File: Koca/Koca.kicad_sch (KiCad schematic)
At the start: 160 parts, among them J1 USB_C_Receptacle, J2 AudioJack4, J3 Conn_01x04_Pin, J4 Conn_01x04_Pin, J5 USB_C_Receptacle, J6 AudioJack4, J7 Conn_01x04_Pin, J8 Conn_01x04_Pin, SW1 SW_Push, SW10 SW_Push, SW11 SW_Push, SW12 SW_Push, SW13 SW_Push, SW14 SW_Push, SW15 SW_Push, SW16 SW_Push, SW17 SW_Push, SW18 SW_Push, SW19 SW_Push, SW2 SW_Push, SW20 SW_Push, SW21 SW_Push, SW22 SW_Push, SW23 SW_Push, SW24 SW_Push, SW25 SW_Push, SW26 SW_Push, SW27 SW_Push, SW28 SW_Push, SW29 SW_Push, SW3 SW_Push, SW30 SW_Push, SW31 SW_Push, SW32 SW_Push, SW33 SW_Push, SW34 SW_Push, SW35 SW_Push, SW36 SW_Push, SW37 SW_Push, SW38 SW_Push, SW39 SW_Push, SW4 SW_Push, SW40 SW_Push, SW41 SW_Push, SW42 SW_Push, SW43 SW_Push, SW44 SW_Push, SW45 SW_Push, SW46 SW_Push, SW47 SW_Push, SW48 SW_Push, SW49 SW_Push, SW5 SW_Push, SW50 SW_Push, SW51 SW_Push, SW52 SW_Push, SW53 SW_Push, SW54 SW_Push, SW55 SW_Push, SW56 SW_Push, SW57 SW_Push, SW58 SW_Push, SW59 SW_Push, SW6 SW_Push, SW60 SW_Push, SW7 SW_Push, SW8 SW_Push, SW9 SW_Push, U1 AMS1117-3.3, U2 USBLC6-2SC6, U3 USBLC6-2SC6, U4 STM32F103RCTx, U5 AMS1117-3.3, U6 USBLC6-2SC6, U7 USBLC6-2SC6, U8 STM32F103RCTx, Y1 12Mhz, Y2 12Mhz

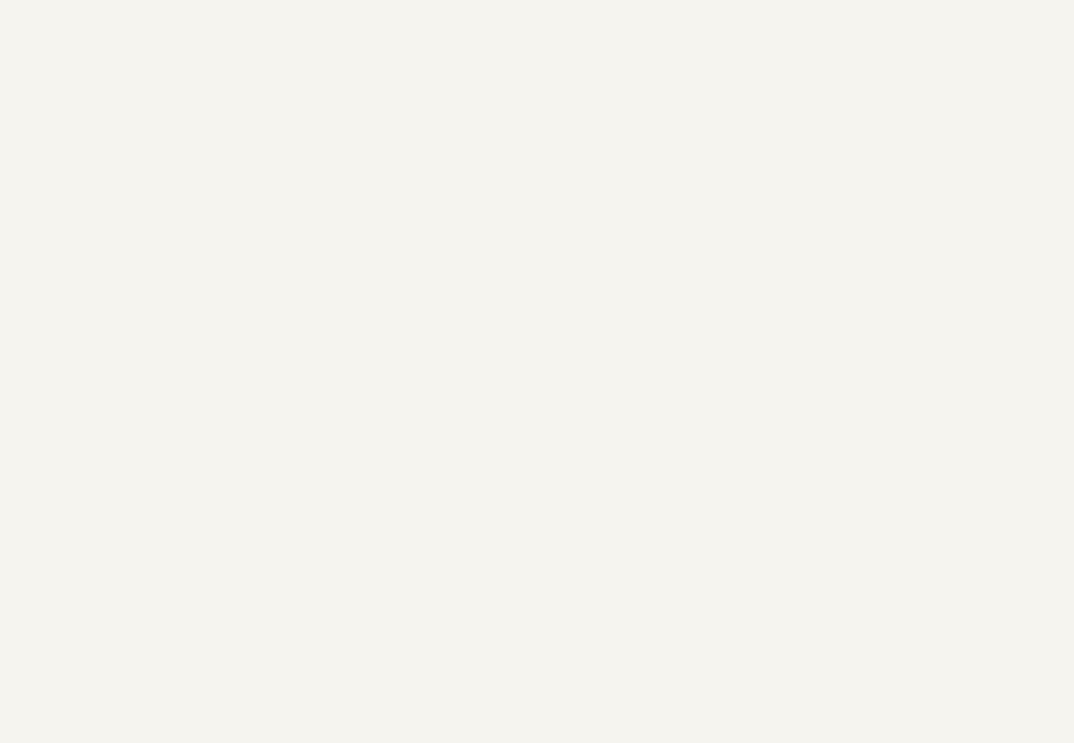
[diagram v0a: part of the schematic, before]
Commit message: Bout to imrpove hotplug protection
Making a commit now because I have some new changes and I want something
to fall back on if the new design changes suck.
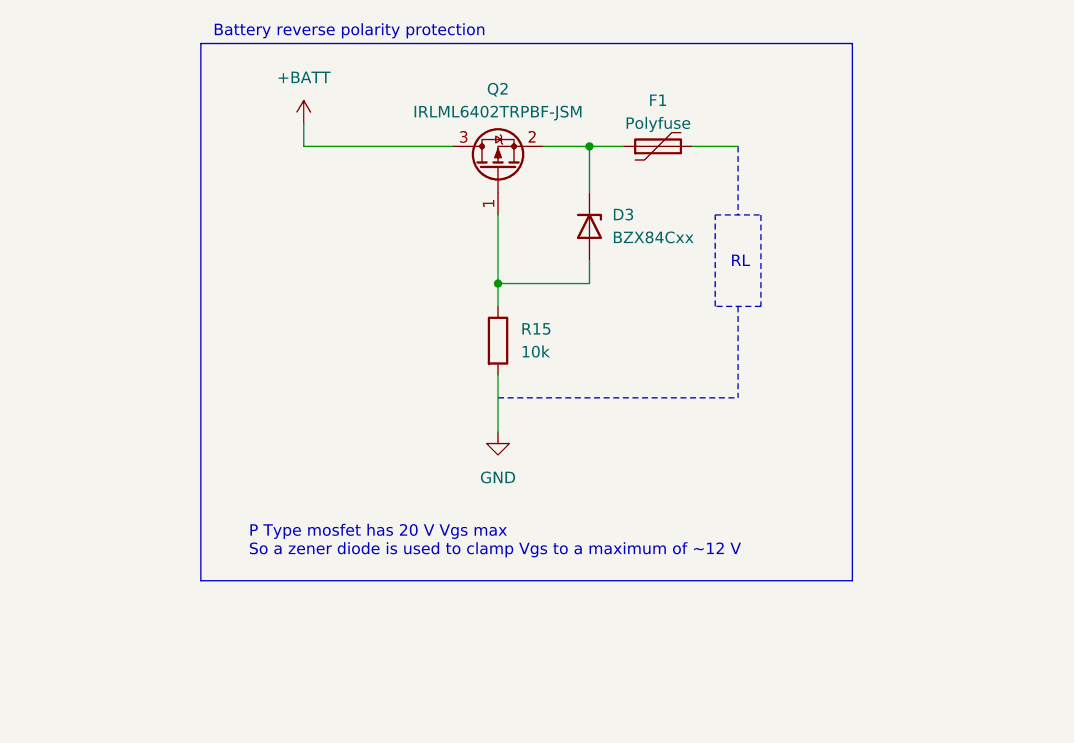
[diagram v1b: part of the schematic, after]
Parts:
- added D3: BZX84Cxx, Package_TO_SOT_SMD:SOT-23, symbol Diode:BZX84Cxx
- added F1: Polyfuse, symbol Device:Polyfuse
- added Q2: IRLML6402TRPBF-JSM, Package_TO_SOT_SMD:SOT-23, symbol Transistor_FET:AO3401A
- added R15: 10k, Resistor_SMD:R_0603_1608Metric, symbol Device:R
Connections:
- net GND: now also R15.2
- new net: D3.1 (A), Q2.1 (G), R15.1
- new net: D3.3 (K), F1.1, Q2.2 (S)
- new net +BATT: Q2.3 (D)
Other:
- note added: "Battery reverse polarity protection"
- note added: "P Type mosfet has 20 V Vgs max So a zener diode is used to clamp Vgs to a maximum of ~12 V"
- note added: "RL"

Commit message: Added hotplugging protection to TRRS
Technically added hotplugging protection. But it won't work because
current isn't able to flow both directions in this design. It would
require one side to always be the slave. But the hotplug protection for
the master would then suck. So I'm about to try switch to USB-C for the
interconnect.
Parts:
- removed D3: BZX84Cxx, Package_TO_SOT_SMD:SOT-23, symbol Diode:BZX84Cxx
- removed J6: AudioJack4, Koca:TRRS-PJ-320A, symbol Connector:AudioJack4
- removed U6: USBLC6-2SC6, Package_TO_SOT_SMD:SOT-23-6, symbol Power_Protection:USBLC6-2SC6
- added D2, D5: BZT52B11, Diode_SMD:D_SOD-123F, symbol Diode:BZT52Bxx
- added D3, D6: SMF6.0CA, Diode_SMD:D_SOD-123F, symbol Device:D_TVS
- added F2: Polyfuse, Fuse:Fuse_0603_1608Metric, symbol Device:Polyfuse
- added J8: AudioJack4, Koca:TRRS-PJ-320A, symbol Connector:AudioJack4
- added Q2: IRLML6402TRPBF-JSM, Package_TO_SOT_SMD:SOT-23, symbol Transistor_FET:AO3401A
- added R16: 10k, Resistor_SMD:R_0402_1005Metric, symbol Device:R
- added U8: USBLC6-2SC6, Package_TO_SOT_SMD:SOT-23-6, symbol Power_Protection:USBLC6-2SC6
- F1: footprint (none) -> Fuse:Fuse_0603_1608Metric
- R8: renamed from R15; footprint Resistor_SMD:R_0603_1608Metric -> Resistor_SMD:R_0402_1005Metric
- renumbered D2 to D4, J3 to J2, J4 to J3, J2 to J4, J7 to J6, J8 to J7, Q2 to Q1, R9 to R10, R10 to R11, R11 to R12, R12 to R13, R13 to R14, R14 to R15, R8 to R9, SW7 to SW1, SW1 to SW2, SW2 to SW3, SW3 to SW4, SW4 to SW5, SW5 to SW6, SW6 to SW7, U4 to U3, U3 to U4, U7 to U6, U8 to U7
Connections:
- net +5V: now also F1.2; no longer J1.A4 (VBUS), J1.A9 (VBUS), J1.B4 (VBUS), J1.B9 (VBUS), J4.T
- net +5VA: now also F2.2, U8.5 (VBUS); no longer J5.A4 (VBUS), J5.A9 (VBUS), J5.B4 (VBUS), J5.B9 (VBUS)
- net GND: now also D3.1 (A1)
- net GNDA: now also D6.1 (A1), J8.S, R16.2, U8.2 (GND)
- net RX_R: now also J8.R2, U8.1 (I/O1), U8.6 (I/O1)
- net TX_R: now also J8.R1, U8.3 (I/O2), U8.4 (I/O2)
- net L_GATE: now reaches Q1.1 (G), R8.1
- net L_GATE: now also D2.2 (A)
- net VDC: now reaches F1.1, Q1.2 (S)
- net VDC: now also J1.A4 (VBUS), J1.A9 (VBUS), J1.B4 (VBUS), J1.B9 (VBUS), D2.1 (K)
- net +BATT renamed V_LJ
- net V_LJ: now also J4.T, D3.2 (A2)
- new net R_GATE: D5.2 (A), Q2.1 (G), R16.1
- new net VBUS: D5.1 (K), F2.1, J5.A4 (VBUS), J5.A9 (VBUS), J5.B4 (VBUS), J5.B9 (VBUS), Q2.2 (S)
- new net V_RJ: D6.2 (A2), J8.T, Q2.3 (D)
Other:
- note added: "Data ESD protection"
- note added: "Hot plug protection"
- note removed: "Battery reverse polarity protection"
- moved on the sheet: C1, C10, C11, C12, C13, C14, C15, C16, C17, C18, C19, C2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

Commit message: Switch to RJ45 Interconnects
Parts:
- removed C12, C26: 100n, Capacitor_SMD:C_0402_1005Metric, symbol Device:C
- removed D2, D5: BZT52B11, Diode_SMD:D_SOD-123F, symbol Diode:BZT52Bxx
- removed D3, D6: SMF6.0CA, Diode_SMD:D_SOD-123F, symbol Device:D_TVS
- removed J1, J5: USB_C_Receptacle, Koca:USB_TYPE-C-31-M-12, symbol Connector:USB_C_Receptacle
- removed J4, J8: AudioJack4, Koca:TRRS-PJ-320A, symbol Connector:AudioJack4
- removed Q1, Q2: IRLML6402TRPBF-JSM, Package_TO_SOT_SMD:SOT-23, symbol Transistor_FET:AO3401A
- removed R10: 5k1, Resistor_SMD:R_0402_1005Metric, symbol Device:R
- removed R14: 1k5, Resistor_SMD:R_0402_1005Metric, symbol Device:R
- removed U4, U6, U8: USBLC6-2SC6, Package_TO_SOT_SMD:SOT-23-6, symbol Power_Protection:USBLC6-2SC6
- added J1, J5: USB_C_Receptacle_USB2.0_16P, Koca:USB_TYPE-C-31-M-12, symbol Connector:USB_C_Receptacle_USB2.0_16P
- added J10: RJ45_LED_Shielded, Connector_RJ:RJ45_Amphenol_RJHSE538X, symbol Connector:RJ45_LED_Shielded
- added J11, J12: RJ45, Koca:RJ45_Amphenol_54602-x08_Horizontal, symbol Connector:RJ45
- added R11, R12: 5k1, Resistor_SMD:R_0402_1005Metric, symbol Device:R
- added R13: 1k5, Resistor_SMD:R_0402_1005Metric, symbol Device:R
- added R18: 4.7, Resistor_SMD:R_0603_1608Metric, symbol Device:R
- added R19, R6: 470, Resistor_SMD:R_0402_1005Metric, symbol Device:R
- added U3, U5, U7: USBLC6-2SC6, Package_TO_SOT_SMD:SOT-23-6, symbol Power_Protection:USBLC6-2SC6
- R16: value 10k -> 470
- R8: value 10k -> 4.7; footprint Resistor_SMD:R_0402_1005Metric -> Resistor_SMD:R_0603_1608Metric
- R9: value 5k1 -> 470
- U4: renamed from U1; footprint Package_TO_SOT_SMD:SOT-223-3_TabPin2 -> Package_TO_SOT_SMD:SOT-89-3
- U8: renamed from U5; footprint Package_TO_SOT_SMD:SOT-223-3_TabPin2 -> Package_TO_SOT_SMD:SOT-89-3
- renumbered C3 to C1, C13 to C10, C14 to C11, C1 to C12, C2 to C13, C17 to C14, C18 to C15, C19 to C16, C20 to C17, C21 to C18, C22 to C19, C4 to C2, C23 to C20, C24 to C21, C25 to C22, C27 to C23, C28 to C24, C15 to C25, C16 to C26, C5 to C3, C6 to C4, C7 to C5, C8 to C6, C9 to C7, C10 to C8, C11 to C9, D4 to D2, JP2 to JP1, JP1 to JP2, JP4 to JP3, JP3 to JP4, R3 to R10, R12 to R14, R13 to R15, R15 to R17, R11 to R20, R6 to R3, U2 to U1, U3 to U2, U7 to U6
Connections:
- net +3.3VA: now also R13.1
- net +5V: no longer U1.5 (VBUS)
- net GND: now also J1.A1 (GND), J1.A12 (GND), J1.B1 (GND), J1.B12 (GND), J1.S1 (SHIELD), J12.7, J12.8, U3.2 (GND); no longer R8.2
- net GNDA: now also J11.7, J11.8, J5.A1 (GND), J5.A12 (GND), J5.B1 (GND), J5.B12 (GND), J5.S1 (SHIELD), R11.1, R12.1, U5.2 (GND), U7.2 (GND); no longer R16.2, R9.1
- net RX_L: now also U3.1 (I/O1)
- net RX_R: now also U7.1 (I/O1)
- net R_D+: now also R13.2, U5.4 (I/O2)
- net R_D-: now also U5.6 (I/O1)
- net TX_L: now also U3.3 (I/O2)
- net TX_R: now also U7.3 (I/O2)
- net VBUS: now also J5.A4 (VBUS), J5.A9 (VBUS), J5.B4 (VBUS), J5.B9 (VBUS), R18.2, U5.5 (VBUS), U7.5 (VBUS)
- net VDC: now also R8.2, U1.5 (VBUS), J1.A4 (VBUS), J1.A9 (VBUS), J1.B4 (VBUS), J1.B9 (VBUS), U3.5 (VBUS)
- net L_CC1: now reaches R1.2
- net L_CC1: now also J1.A5 (CC1)
- net L_CC2: now reaches R2.2
- net L_CC2: now also J1.B5 (CC2)
- net at R9.2: now also U3.4 (I/O2)
- net L_K: now reaches D1.1 (K), R10.1
- net R_K: now reaches D2.1 (K), R20.1
- net R_A: now reaches D2.2 (A), JP4.2 (B)
- net L_A: now reaches D1.2 (A), JP2.2 (B)
- net CON_DM_L renamed LCON_D-
- net LCON_D-: now also J1.A7 (D-), J1.B7 (D-)
- net CON_DP_L renamed LCON_D+
- net LCON_D+: now also J1.A6 (D+), J1.B6 (D+)
- net L_GATE renamed LCON_V
- net LCON_V: now also J12.4, J12.5
- net R_GATE renamed CON_RX_R
- net CON_RX_R: now also J11.1
- new net: R19.2, U7.4 (I/O2)
- new net: R16.2, U7.6 (I/O1)
- new net: R6.2, U3.6 (I/O1)
- new net CON_RX_L: J12.2, R6.1
- new net CON_TX_L: J12.1, R9.1
- new net CON_TX_R: J11.2, R19.1
- new net RCON_D+: J5.A6 (D+), J5.B6 (D+), U5.3 (I/O2)
- new net RCON_D-: J5.A7 (D-), J5.B7 (D-), U5.1 (I/O1)
- new net RCON_V: J11.4, J11.5, R18.1
- new net R_CC1: J5.A5 (CC1), R11.2
- new net R_CC2: J5.B5 (CC2), R12.2
- no-connect marks 62 -> 50
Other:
- note added: "Keyboard interconnect"
- note added: "Main ESD protection"
- note added: "USART protection"
- note removed: "Data ESD protection"
- note removed: "Hot plug protection"
- note removed: "P Type mosfet has 20 V Vgs max So a zener diode is used to clamp Vgs to a maximum of ~12 V"
- note removed: "RL"
- note removed: "TRRS"
- company: (none) -> oxnh
- moved on the sheet: C12, C13, C25, C26, D1, D2, F1, JP2, JP4, R1, R10, R2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
